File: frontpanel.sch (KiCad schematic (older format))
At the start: 4 parts

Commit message: wip
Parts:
- added R?: R, symbol Device:R
- added U1: 74HC04, symbol 74xx:74HC04
- added U119: PCF8574, symbol Interface_Expansion:PCF8574
- gave numbers to parts that had none: 4
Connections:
- net GND: now also U119.1 (A0), U119.2 (A1), U119.3 (A2)
- net at U96.1 (PA6): now also J2.19 (Pin_19)
- net at U96.2 (PA5): now also J2.12 (Pin_12)
- net at J2.17 (Pin_17), U96.29 (MISO/PD2): now also U119.11 (P6)
- net at J2.10 (Pin_10), U96.30 (MOSI/PD3): now also U119.5 (P1)
- net at J2.11 (Pin_11), U118.11 (SCLK), U2.11 (SCLK)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: now also U119.6 (P2)
- net at J2.14 (Pin_14), U96.32 (SS/PD5): now also U119.10 (P5)
- net at U96.34 (PD7): now also J2.8 (Pin_8), U118.13 (~G), U2.13 (~G)
- net at U96.41 (~RESET): now also J2.13 (Pin_13)
- net at U96.44 (PA7): now also J2.18 (Pin_18), R?.2
- net at U118.10 (~SCLR): now also U2.10 (~SCLR), U1.6
- net at U118.12 (RCLK): now also U2.12 (RCLK), U2.9 (QHser), U1.1
- new net: U1.2, U1.3
- new net: U1.4, U1.5
- new net +3V3: R?.1
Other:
- note added: "PCF8574 has SSOP20 Footprint on the PCB. \nIn this schemtic the Pins are translated to SO16\n"
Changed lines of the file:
@@
 $EndDescr
 $Comp
-L MCU_NXP_HC11:MC68HC705_44pin U?
+L MCU_NXP_HC11:MC68HC705_44pin U96
 U 1 1 5F95D5D4
 P 4600 5550
-F 0 "U?" H 5744 5571 50  0000 L CNN
+F 0 "U96" H 5744 5571 50  0000 L CNN
 F 1 "MC68HC705_44pin" H 5744 5480 50  0000 L CNN
 F 2 "" H 4900 3600 50  0001 C CNN
@@
 $EndComp
 $Comp
-L Connector:Conn_01x22_Female J?
+L Connector:Conn_01x22_Female J2
 U 1 1 5F95E964
 P 1650 2850
-F 0 "J?" H 1542 4035 50  0000 C CNN
+F 0 "J2" H 1542 4035 50  0000 C CNN
 F 1 "Conn_01x22_Female" H 1542 3944 50  0000 C CNN
 F 2 "" H 1650 2850 50  0001 C CNN
@@
 $EndComp
 Wire Wire Line
-	1850 2750 4250 2750
+	1850 2750 2250 2750
 Wire Wire Line
 	4250 2750 4250 4450
 Wire Wire Line
-	1850 2850 4100 2850
+	1850 2850 2350 2850
 Wire Wire Line
 	4100 2850 4100 4450
 Wire Wire Line
-	1850 3150 3950 3150
+	1850 3150 2450 3150
 Wire Wire Line
 	3950 3150 3950 4450
 Wire Wire Line
-	1850 3450 4400 3450
+	1850 3450 2600 3450
 Wire Wire Line
 	4400 3450 4400 4450
 $Comp
-L 74xx_IEEE:74LS594 U?
+L 74xx_IEEE:74LS594 U118
 U 1 1 5F969872
 P 7300 2250
-F 0 "U?" H 7300 3066 50  0000 C CNN
+F 0 "U118" H 7300 3066 50  0000 C CNN
 F 1 "74LS594" H 7300 2975 50  0000 C CNN
 F 2 "" H 7300 2250 50  0001 C CNN
@@
 $EndComp
 $Comp
-L 74xx_IEEE:74LS594 U?
+L 74xx_IEEE:74LS594 U2
 U 1 1 5F96B299
 P 7300 4150
-F 0 "U?" H 7300 4966 50  0000 C CNN
+F 0 "U2" H 7300 4966 50  0000 C CNN
 F 1 "74LS594" H 7300 4875 50  0000 C CNN
 F 2 "" H 7300 4150 50  0001 C CNN
@@
 	6500 4550 6750 4550
 Wire Wire Line
-	1850 2650 6750 2650
-Wire Wire Line
 	4100 2850 5900 2850
 Wire Wire Line
@@
 Wire Wire Line
 	6100 3600 6750 3600
-Wire Wire Line
-	6100 1700 6100 2550
-Wire Wire Line
-	1850 2550 6100 2550
-Connection ~ 6100 2550
-Wire Wire Line
-	6100 2550 6100 3600
 $Comp
 L power:GND #PWR?
@@
 Wire Wire Line
 	1950 3950 1950 4150
-Wire Wire Line
-	1850 3250 1950 3250
-Wire Wire Line
-	1950 3250 1950 3850
 Connection ~ 1950 3850
 Wire Wire Line
 	1950 3850 1950 3950
 Wire Wire Line
-	1850 2450 1950 2450
-Wire Wire Line
-	1950 2450 1950 3250
-Connection ~ 1950 3250
-Wire Wire Line
 	1850 2050 1950 2050
-Wire Wire Line
-	1950 2050 1950 2450
-Connection ~ 1950 2450
 Wire Wire Line
 	1850 1950 1950 1950
@@
 	1950 1850 1950 1950
 Connection ~ 1950 1950
+$Comp
+L 74xx:74HC04 U1
+U 1 1 5F99A5DD
+P 7050 5650
+F 0 "U1" H 7050 5967 50  0000 C CNN
+F 1 "74HC04" H 7050 5876 50  0000 C CNN
+F 2 "" H 7050 5650 50  0001 C CNN
+F 3 "https://assets.nexperia.com/documents/data-sheet/74HC_HCT04.pdf" H 7050 5650 50  0001 C CNN
+	1    7050 5650
+	1    0    0    -1
+$EndComp
+$Comp
+L 74xx:74HC04 U1
+U 2 1 5F99B9B9
+P 7650 5650
+F 0 "U1" H 7650 5967 50  0000 C CNN
+F 1 "74HC04" H 7650 5876 50  0000 C CNN
+F 2 "" H 7650 5650 50  0001 C CNN
+F 3 "https://assets.nexperia.com/documents/data-sheet/74HC_HCT04.pdf" H 7650 5650 50  0001 C CNN
+	2    7650 5650
+	1    0    0    -1
+$EndComp
+$Comp
+L 74xx:74HC04 U1
+U 3 1 5F99C92C
+P 8250 5650
+F 0 "U1" H 8250 5967 50  0000 C CNN
+F 1 "74HC04" H 8250 5876 50  0000 C CNN
+F 2 "" H 8250 5650 50  0001 C CNN
+F 3 "https://assets.nexperia.com/documents/data-sheet/74HC_HCT04.pdf" H 8250 5650 50  0001 C CNN
+	3    8250 5650
+	1    0    0    -1
+$EndComp
+Wire Wire Line
+	8550 5650 8550 6450
+Wire Wire Line
+	6300 1950 6300 3850
+Wire Wire Line
+	6300 3850 6750 3850
+Wire Wire Line
+	6300 1950 6750 1950
+Wire Wire Line
+	6650 3700 6650 1800
+Wire Wire Line
+	6650 1800 6750 1800
+Wire Wire Line
+	6750 5650 6650 5650
+Wire Wire Line
+	6650 5650 6650 5150
+Connection ~ 6650 3700
+Wire Wire Line
+	8550 6450 6300 6450
+Wire Wire Line
+	6300 6450 6300 3850
+Connection ~ 6300 3850
+$Comp
+L Interface_Expansion:PCF8574 U119
+U 1 1 5F9C17F7
+P 1450 5500
+F 0 "U119" H 1450 6381 50  0000 C CNN
+F 1 "PCF8574" H 1450 6290 50  0000 C CNN
+F 2 "" H 1450 5500 50  0001 C CNN
+F 3 "http://www.nxp.com/documents/data_sheet/PCF8574_PCF8574A.pdf" H 1450 5500 50  0001 C CNN
+	1    1450 5500
+	1    0    0    -1
+$EndComp
+Wire Wire Line
+	1950 5200 2250 5200
+Wire Wire Line
+	6650 3700 6750 3700
+Wire Wire Line
+	1850 2650 6750 2650
+Wire Wire Line
+	6100 1700 6100 2550
+Wire Wire Line
+	1950 2050 1950 2450
+Wire Wire Line
+	1850 3250 1950 3250
+Connection ~ 1950 3250
+Wire Wire Line
+	1950 3250 1950 3850
+Wire Wire Line
+	1850 2450 1950 2450
+Connection ~ 1950 2450
+Wire Wire Line
+	1950 2450 1950 3250
+Wire Wire Line
+	1850 2550 3450 2550
+Wire Wire Line
+	3450 2550 3450 4750
+Wire Wire Line
+	3450 2550 6100 2550
+Connection ~ 3450 2550
+Connection ~ 6100 2550
+Wire Wire Line
+	6100 2550 6100 3600
+Wire Wire Line
+	1850 3050 3050 3050
+Wire Wire Line
+	3450 5800 3050 5800
+Wire Wire Line
+	3050 3050 3050 5800
+Wire Wire Line
+	2350 2850 2350 5300
+Wire Wire Line
+	1950 5300 2350 5300
+Connection ~ 2350 2850
+Wire Wire Line
+	2350 2850 4100 2850
+Wire Wire Line
+	2250 5200 2250 2750
+Connection ~ 2250 2750
+Wire Wire Line
+	2250 2750 4250 2750
+Wire Wire Line
+	2450 3150 2450 5600
+Wire Wire Line
+	2450 5600 1950 5600
+Connection ~ 2450 3150
+Wire Wire Line
+	2450 3150 3950 3150
+Wire Wire Line
+	2600 3450 2600 5700
+Wire Wire Line
+	2600 5700 1950 5700
+Connection ~ 2600 3450
+Wire Wire Line
+	2600 3450 4400 3450
+$Comp
+L power:GND #PWR?
+U 1 1 5F9E3449
+P 700 6050
+F 0 "#PWR?" H 700 5800 50  0001 C CNN
+F 1 "GND" H 705 5877 50  0000 C CNN
+F 2 "" H 700 6050 50  0001 C CNN
+F 3 "" H 700 6050 50  0001 C CNN
+	1    700  6050
+	1    0    0    -1
+$EndComp
+Wire Wire Line
+	950  5400 700  5400
+Wire Wire Line
+	700  5400 700  5500
+Wire Wire Line
+	950  5500 700  5500
+Connection ~ 700  5500
+Wire Wire Line
+	700  5500 700  5600
+Wire Wire Line
+	950  5600 700  5600
+Connection ~ 700  5600
+Wire Wire Line
+	700  5600 700  6050
+Wire Wire Line
+	1850 2950 2900 2950
+Wire Wire Line
+	2900 2950 2900 7100
+Wire Wire Line
+	2900 7100 4000 7100
+Wire Wire Line
+	4000 7100 4000 6700
+Wire Wire Line
+	1850 3650 3000 3650
+Wire Wire Line
+	3000 3650 3000 6950
+Wire Wire Line
+	3000 6950 3850 6950
+Wire Wire Line
+	3850 6950 3850 6700
+Wire Wire Line
+	1850 3550 2750 3550
+Wire Wire Line
+	2750 6250 3450 6250
+$Comp
+L Device:R R?
+U 1 1 5F9F6ABE
+P 2450 6450
+F 0 "R?" H 2520 6496 50  0000 L CNN
+F 1 "R" H 2520 6405 50  0000 L CNN
+F 2 "" V 2380 6450 50  0001 C CNN
+F 3 "~" H 2450 6450 50  0001 C CNN
+	1    2450 6450
+	1    0    0    -1
+$EndComp
+$Comp
+L power:+3V3 #PWR?
+U 1 1 5F9F7551
+P 2450 6300
+F 0 "#PWR?" H 2450 6150 50  0001 C CNN
+F 1 "+3V3" H 2465 6473 50  0000 C CNN
+F 2 "" H 2450 6300 50  0001 C CNN
+F 3 "" H 2450 6300 50  0001 C CNN
+	1    2450 6300
+	1    0    0    -1
+$EndComp
+Wire Wire Line
+	2450 6600 2750 6600
+Wire Wire Line
+	2750 3550 2750 6250
+Connection ~ 2750 6250
+Wire Wire Line
+	2750 6250 2750 6600
+Wire Wire Line
+	7850 4950 7850 5150
+Wire Wire Line
+	7850 5150 6650 5150
+Connection ~ 6650 5150
+Wire Wire Line
+	6650 5150 6650 3700
+Text Notes 600  6850 0    50   ~ 0
+PCF8574 has SSOP20 Footprint on the PCB. \nIn this schemtic the Pins are translated to SO16\n
 $EndSCHEMATC

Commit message: wip
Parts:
- added R? (x2): 10k, symbol Device:R
- R?: value R -> 10k
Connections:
- net +3V3: now also U96.38 (VDD), U96.42 (~IRQ), U96.43 (Vpp), R?.1, R?.1
- net at J2.19 (Pin_19), U96.1 (PA6): now also R?.2
- net at J2.12 (Pin_12), U96.2 (PA5): now also U119.7 (P3)
- net at J2.17 (Pin_17), U119.11 (P6), U96.29 (MISO/PD2): now also R?.2
- net at J2.13 (Pin_13), U96.41 (~RESET): now also U119.9 (P4)
- net at J2.18 (Pin_18), R?.2, U96.44 (PA7): now also U119.12 (P7)
- net at J2.9 (Pin_9), U118.14 (SER): now also U119.4 (P0)
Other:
- note added: "17 clock cycles are used to set the LEDs.\nthe 17th clock cycle commits the shift register\nstate to the output stage. The 74HC04 Delay-Line\nresets the shift register afterwards"
- note added: "Observation: Pins of the MC68HC705 that are companioned\nby a 10k-PullUp might be used as outputs. This assumption\nis made because MISO also has a pullup."
- note added: "PA7 (Pin 18 on J2) is a possible candidate for signaling\nEncoder/PushButton changes to the PCI-Board"
- note added: "U119 (PCF8574) provides an alternative but deprecated \nI2C-communications interface between the PCI-Board\nand the Frontpanel\n"
- moved on the sheet: R?, U1A, U1B, U1C, U2, U96

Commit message: some labeling
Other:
- note added: "CS/"
- note added: "MISO"
- note added: "MOSI"
- note added: "PA6"
- note added: "PA7"
- note added: "PD7"
- note added: "RESET/"
- note added: "SCK"
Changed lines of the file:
@@
 Text GLabel 6050 7300 2    50   Input ~ 0
 ?Matrix_Encoder
+Text Notes 1450 3450 0    50   ~ 0
+MISO
+Text Notes 1450 2750 0    50   ~ 0
+MOSI
+Text Notes 1450 2850 0    50   ~ 0
+SCK
+Text Notes 1450 3150 0    50   ~ 0
+CS/
+Text Notes 1350 3050 0    50   ~ 0
+RESET/
+Text Notes 1450 3550 0    50   ~ 0
+PA7
+Text Notes 1450 2550 0    50   ~ 0
+PD7
+Text Notes 1450 3650 0    50   ~ 0
+PA6
 $EndSCHEMATC

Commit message: added crystal
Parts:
- added Y?: 3.687Mhz, symbol Device:Crystal
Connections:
- net at U96.36 (OSC2): now also Y?.1
- net at U96.37 (OSC1): now also Y?.2
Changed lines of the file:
@@
 Text Notes 1450 3650 0    50   ~ 0
 PA6
+$Comp
+L Device:Crystal Y?
+U 1 1 5FD369AC
+P 4200 5050
+F 0 "Y?" V 4154 5181 50  0000 L CNN
+F 1 "3.687Mhz" V 4245 5181 50  0000 L CNN
+F 2 "" H 4200 5050 50  0001 C CNN
+F 3 "~" H 4200 5050 50  0001 C CNN
+	1    4200 5050
+	0    1    1    0
+$EndComp
+Wire Wire Line
+	4550 5050 4450 5050
+Wire Wire Line
+	4450 5050 4450 4900
+Wire Wire Line
+	4450 4900 4200 4900
+Wire Wire Line
+	4550 5200 4200 5200
 $EndSCHEMATC

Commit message: some annotations
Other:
- note added: "According to Diodes used in the Encoder Matrix this should be inputs."
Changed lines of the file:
@@
 Wire Wire Line
 	4550 5200 4200 5200
+Text Notes 7200 4700 0    50   ~ 0
+According to Diodes used in the Encoder Matrix this should be inputs.
 $EndSCHEMATC

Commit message: added connection diagram to LPC47N227
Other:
- note added: "LED_DATA"
- note added: "LPC47N227 on PCI-Card"
- note added: "PA5\n"
- note added: "Pin 32 - GP30"
- note added: "Pin 33 - GP31"
- note added: "Pin 34 - GP32"
- note added: "Pin 35 - GP33"
- note added: "Pin 36 - GP34"
- note added: "Pin 37 - GP35"
- note added: "Pin 40 - GP 40"
- note added: "Pin 41 - GP 41"
- note added: "Pin 47 - GP 47"
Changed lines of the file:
@@
 Text Notes 7200 4700 0    50   ~ 0
 According to Diodes used in the Encoder Matrix this should be inputs.
+Text Notes 1450 2950 0    50   ~ 0
+PA5\n
+Text Notes 1250 2650 0    50   ~ 0
+LED_DATA
+Text Notes 550  2650 0    50   ~ 0
+Pin 32 - GP30
+Text Notes 550  2750 0    50   ~ 0
+Pin 33 - GP31
+Text Notes 550  2850 0    50   ~ 0
+Pin 34 - GP32
+Text Notes 550  2950 0    50   ~ 0
+Pin 35 - GP33
+Text Notes 550  3050 0    50   ~ 0
+Pin 36 - GP34
+Text Notes 550  3150 0    50   ~ 0
+Pin 37 - GP35
+Text Notes 550  3450 0    50   ~ 0
+Pin 47 - GP 47
+Text Notes 550  3550 0    50   ~ 0
+Pin 41 - GP 41
+Text Notes 550  3650 0    50   ~ 0
+Pin 40 - GP 40
+Text Notes 550  3600 1    50   ~ 0
+LPC47N227 on PCI-Card
 $EndSCHEMATC

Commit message: added PA7 connection
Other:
- note added: "Pin 39 - GP37"
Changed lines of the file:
@@
 Text Notes 550  3600 1    50   ~ 0
 LPC47N227 on PCI-Card
+Text Notes 550  2550 0    50   ~ 0
+Pin 39 - GP37
 $EndSCHEMATC

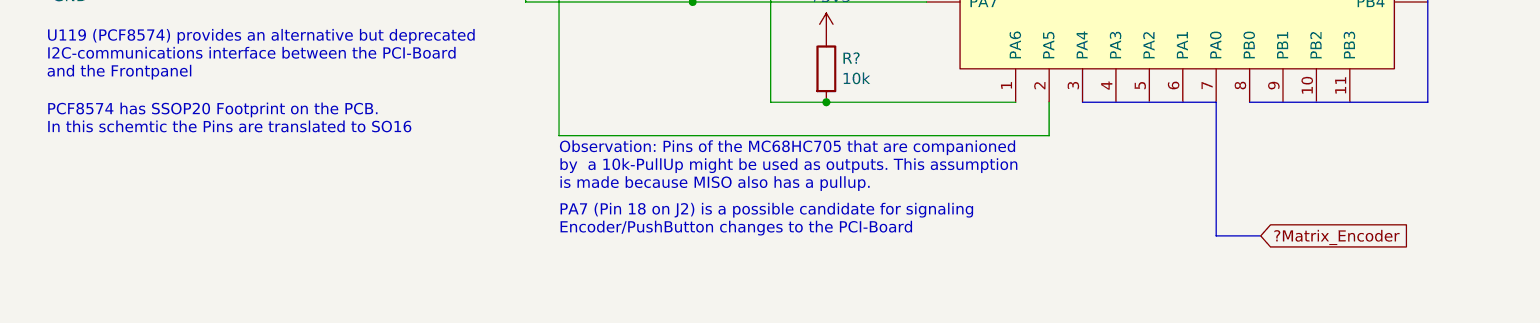
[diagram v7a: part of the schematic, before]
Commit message: pa6 is some kind of disable signal
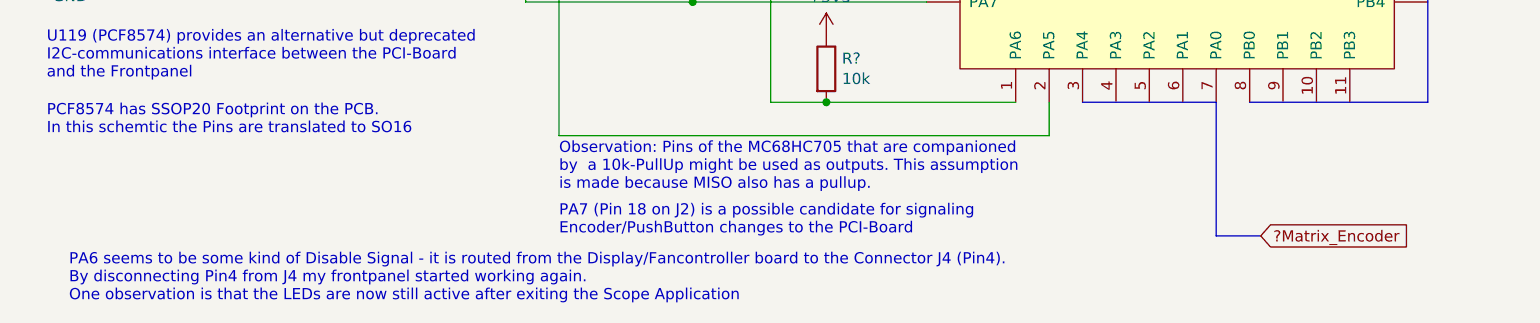
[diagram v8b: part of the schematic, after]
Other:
- note added: "PA6 seems to be some kind of Disable Signal - it is routed from the Display/Fancontroller board to the Connector J4 (Pin4).\nBy disconnecting Pin4 from J4 my frontpanel started working again.\nOne observation is that the LEDs are now still active after exiting the Scope Application\n"
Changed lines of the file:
@@
 Text Notes 550  2550 0    50   ~ 0
 Pin 39 - GP37
+Text Notes 700  7600 0    50   ~ 0
+PA6 seems to be some kind of Disable Signal - it is routed from the Display/Fancontroller board to the Connector J4 (Pin4).\nBy disconnecting Pin4 from J4 my frontpanel started working again.\nOne observation is that the LEDs are now still active after exiting the Scope Application\n
 $EndSCHEMATC
